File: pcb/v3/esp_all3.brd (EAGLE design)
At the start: 45 x 95 mm, 23 parts

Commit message: updated schematic
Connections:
- net N$25 renamed 3V3
- net N$26 renamed DHT_SIG
- net N$28 renamed TTL_DIMM
- removed net N$23: ESP.D5, ESP.D51
- removed net N$29: ESP.D1, ESP.D11, PIR.2
- new net N$16: ESP.D1, ESP.D11
- new net PIR: ESP.D5, ESP.D51, PIR.2
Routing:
- net PIR: track 0.00 -> 66.7 mm, vias 0 -> 2
- net N$29: track 51.9 -> 0.00 mm, vias 2 -> 0
- net N$23: track 2.47 -> 0.00 mm
- net N$16: track 0.00 -> 2.47 mm
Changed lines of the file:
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@@
 <wire x1="37.12" y1="25.18" x2="38.3" y2="24" width="0.4064" layer="1"/>
 </signal>
-<signal name="N$23">
+<signal name="PIR">
 <contactref element="ESP" pad="D5"/>
 <contactref element="ESP" pad="D51"/>
 <wire x1="31.1" y1="32.8" x2="28.63" y2="32.8" width="0.4064" layer="1"/>
-</signal>
-<signal name="N$26">
+<contactref element="PIR" pad="2"/>
+<wire x1="13.26" y1="48.04" x2="13.2" y2="48.1" width="0.4064" layer="1"/>
+<via x="13.2" y="48.1" extent="1-16" drill="0.3048"/>
+<wire x1="13.2" y1="48.1" x2="12.8" y2="48.5" width="0.4064" layer="16"/>
+<wire x1="12.8" y1="48.5" x2="12.8" y2="58.4" width="0.4064" layer="16"/>
+<wire x1="12.8" y1="58.4" x2="10.6" y2="60.6" width="0.4064" layer="16"/>
+<wire x1="28.63" y1="32.8" x2="29.9" y2="34.07" width="0.4064" layer="16"/>
+<wire x1="29.9" y1="34.07" x2="29.9" y2="46.8" width="0.4064" layer="16"/>
+<via x="29.9" y="46.8" extent="1-16" drill="0.3048"/>
+<wire x1="29.9" y1="46.8" x2="21.1" y2="46.8" width="0.4064" layer="1"/>
+<wire x1="21.1" y1="46.8" x2="19.8" y2="48.1" width="0.4064" layer="1"/>
+<wire x1="19.8" y1="48.1" x2="13.2" y2="48.1" width="0.4064" layer="1"/>
+<wire x1="10.6" y1="60.6" x2="10.6" y2="76.36" width="0.4064" layer="16"/>
+<wire x1="10.6" y1="76.36" x2="12.74" y2="78.5" width="0.4064" layer="16"/>
+</signal>
+<signal name="DHT_SIG">
 <contactref element="ESP" pad="D4"/>
 <contactref element="DHT22" pad="2"/>
@@
 <wire x1="15.396" y1="42.96" x2="15.1584" y2="43.1976" width="0.4064" layer="1"/>
 </signal>
-<signal name="N$28">
+<signal name="TTL_DIMM">
 <contactref element="ESP" pad="D2"/>
 <contactref element="DIMMING" pad="1"/>
@@
 <wire x1="19.8" y1="46.3" x2="20.6" y2="45.5" width="0.4064" layer="1"/>
 <wire x1="20.6" y1="45.5" x2="28.63" y2="45.5" width="0.4064" layer="1"/>
-</signal>
-<signal name="N$29">
-<contactref element="ESP" pad="D1"/>
-<contactref element="PIR" pad="2"/>
-<contactref element="ESP" pad="D11"/>
-<wire x1="31.1" y1="48.04" x2="28.63" y2="48.04" width="0.4064" layer="1"/>
-<wire x1="28.63" y1="48.04" x2="13.26" y2="48.04" width="0.4064" layer="1"/>
-<wire x1="13.26" y1="48.04" x2="13.2" y2="48.1" width="0.4064" layer="1"/>
-<via x="13.2" y="48.1" extent="1-16" drill="0.3048"/>
-<wire x1="13.2" y1="48.1" x2="12.8" y2="48.5" width="0.4064" layer="16"/>
-<wire x1="12.8" y1="48.5" x2="12.8" y2="58.4" width="0.4064" layer="16"/>
-<wire x1="12.8" y1="58.4" x2="10.6" y2="60.6" width="0.4064" layer="16"/>
-<via x="10.6" y="60.6" extent="1-16" drill="0.3048"/>
-<wire x1="8.7" y1="71.8" x2="8.7" y2="74.46" width="0.4064" layer="1"/>
-<wire x1="8.7" y1="74.46" x2="12.74" y2="78.5" width="0.4064" layer="1"/>
-<wire x1="10.6" y1="60.6" x2="9.7" y2="61.5" width="0.4064" layer="1"/>
-<wire x1="9.7" y1="61.5" x2="9.7" y2="70.8" width="0.4064" layer="1"/>
-<wire x1="9.7" y1="70.8" x2="8.7" y2="71.8" width="0.4064" layer="1"/>
 </signal>
 <signal name="N$30">
@@
 <contactref element="ESP" pad="3V3@2"/>
 </signal>
-<signal name="N$25">
+<signal name="3V3">
 <contactref element="SV3" pad="1"/>
 <contactref element="SV2" pad="1"/>
@@
 <wire x1="12.8" y1="13.9" x2="12.9" y2="13.8" width="0.4064" layer="1"/>
 </signal>
+<signal name="N$16">
+<contactref element="ESP" pad="D1"/>
+<contactref element="ESP" pad="D11"/>
+<wire x1="31.1" y1="48.04" x2="28.63" y2="48.04" width="0.4064" layer="1"/>
+</signal>
 </signals>

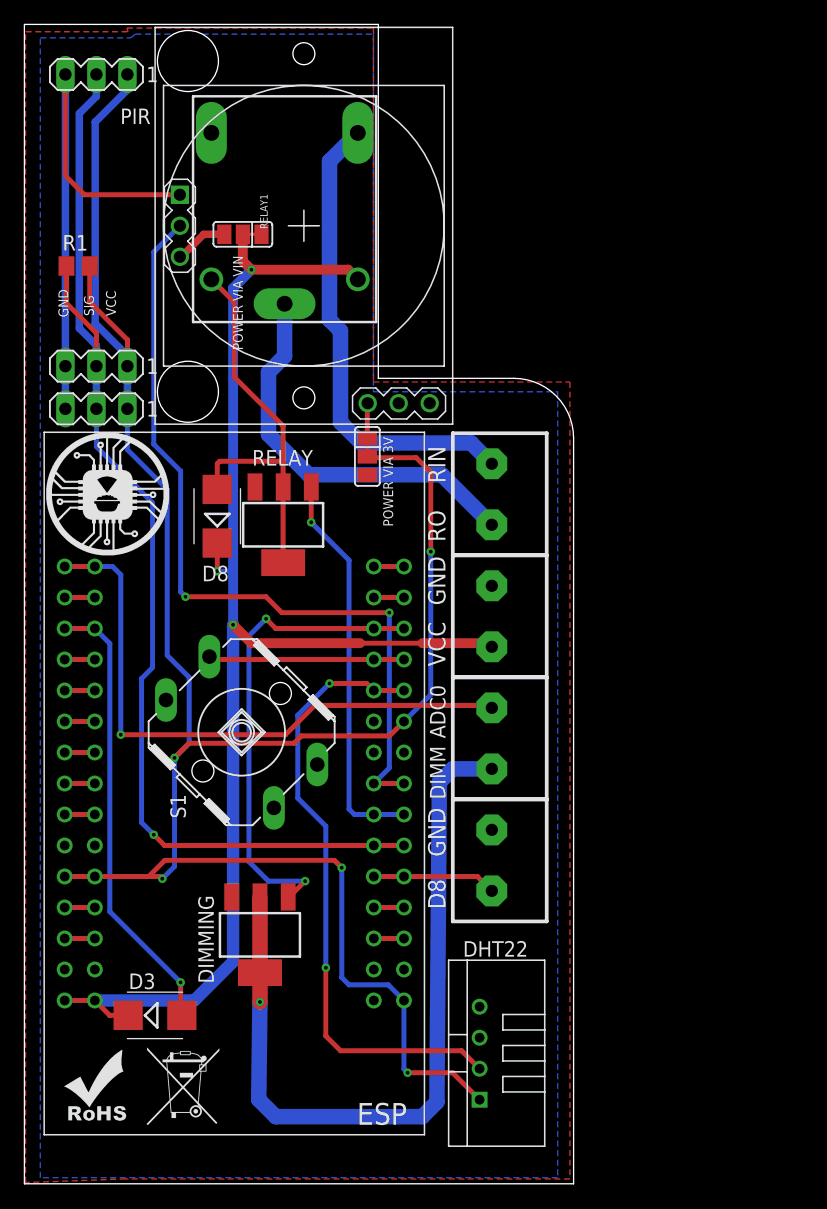
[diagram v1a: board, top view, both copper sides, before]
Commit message: added LDO
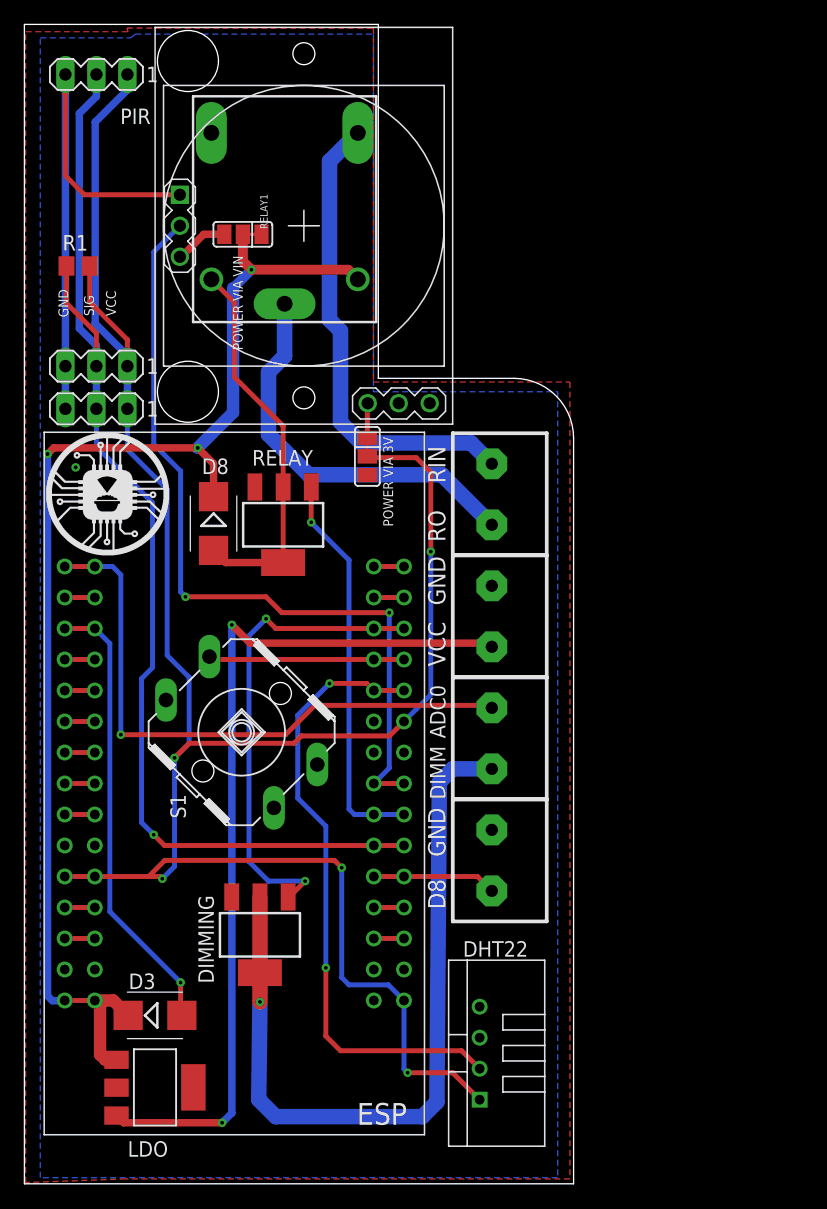
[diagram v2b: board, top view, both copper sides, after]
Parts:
- added LDO: REG1118, burr-brown:SOT223
- moved U$4 25.5 mm to (35.2, 1.20), flipped to the bottom
- moved U$9 23.3 mm to (25.8, 1.50), flipped to the bottom
- moved D8 0.67 mm to (15.5, 54.1), turned to 270 degrees
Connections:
- new net N$17: LDO.3, U$7.P$1
- net GND: now also LDO.2
- net VCC: now also LDO.1; no longer U$7.P$1
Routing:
- net N$17: track 0.00 -> 72.1 mm, vias 0 -> 2
- net VCC: track 113.9 -> 103.5 mm
- net RELAY_LO3: track 33.3 -> 31.9 mm
- net GND: vias 0 -> 1
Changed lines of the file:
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@@
 <text x="41" y="52.6" size="1.4224" layer="26" font="vector" rot="MR90">RO</text>
 <text x="41" y="57.4" size="1.4224" layer="26" font="vector" rot="MR90">RIN</text>
-<text x="16.9" y="2.6" size="1.778" layer="26" font="vector" rot="MR0">SMARTHOME
+<text x="17" y="1.7" size="1.778" layer="26" font="vector" rot="MR0">SMARTHOME
 ESP MQTT
 v03 | 2017</text>
@@
 <attribute name="VALUE" x="23.74" y="55.3208" size="1.27" layer="27" rot="R180"/>
 </element>
-<element name="D8" library="diode" package="SMB" value="ES2D" x="15.8" y="54.7" smashed="yes" rot="R90">
-<attribute name="NAME" x="16.759" y="50.641" size="1.27" layer="25" rot="R180"/>
-<attribute name="VALUE" x="19.229" y="52.541" size="1.27" layer="27" rot="R90"/>
+<element name="D8" library="diode" package="SMB" value="ES2D" x="15.5" y="54.1" smashed="yes" rot="R270">
+<attribute name="NAME" x="14.541" y="58.159" size="1.27" layer="25"/>
+<attribute name="VALUE" x="12.071" y="56.259" size="1.27" layer="27" rot="R270"/>
 </element>
 <element name="U$8" library="JKW_CHIP" package="2_SCREW_PIN" value="V1" x="38.8" y="56.5" rot="R90"/>
@@
 </element>
 <element name="U$1" library="JKW_CHIP" package="LOGO2_10X10_SILK" value="LOGO_10X10_SILK" x="18.8" y="17.4" rot="MR0"/>
-<element name="U$4" library="JKW_CHIP" package="LOGO_ROHS_NO_TRASH" value="LOGO_NO_TRASHNO_TRASH" x="10" y="4.8"/>
-<element name="U$9" library="JKW_CHIP" package="LOGO_ROHS_SYM" value="LOGO_NO_TRASHROHS" x="2.8" y="5.1"/>
+<element name="U$4" library="JKW_CHIP" package="LOGO_ROHS_NO_TRASH" value="LOGO_NO_TRASHNO_TRASH" x="35.2" y="1.2" rot="MR0"/>
+<element name="U$9" library="JKW_CHIP" package="LOGO_ROHS_SYM" value="LOGO_NO_TRASHROHS" x="25.8" y="1.5" rot="MR0"/>
 <element name="U$11" library="JKW_CHIP" package="LOGO2_10X10_SILK" value="LOGO_10X10_SILK" x="1.8" y="51.5"/>
 <element name="D3" library="diode" package="SMB" value="ES2D" x="10.7" y="13.8"/>
+<element name="LDO" library="burr-brown" package="SOT223" value="REG1118" x="10.7" y="7.9" smashed="yes" rot="R270">
+<attribute name="MPN" value="REG1118-2.85/2K5G4" x="10.7" y="7.9" size="1.778" layer="27" rot="R270" display="off"/>
+<attribute name="OC_NEWARK" value="14M2185" x="10.7" y="7.9" size="1.778" layer="27" rot="R270" display="off"/>
+<attribute name="OC_FARNELL" value="unknown" x="10.7" y="7.9" size="1.778" layer="27" rot="R270" display="off"/>
+<attribute name="MF" value="" x="10.7" y="7.9" size="1.778" layer="27" rot="R270" display="off"/>
+<attribute name="NAME" x="8.46" y="2.218" size="1.27" layer="25" ratio="10"/>
+<attribute name="VALUE" x="4.858" y="10.694" size="1.27" layer="27" ratio="10" rot="R270"/>
+</element>
 </elements>
 <signals>
@@
 <wire x1="12.74" y1="81.04" x2="4.92" y2="81.04" width="0.4064" layer="1"/>
 <wire x1="4.92" y1="81.04" x2="3.36" y2="82.6" width="0.4064" layer="1"/>
+<contactref element="LDO" pad="2"/>
+<via x="4.2" y="58.7" extent="1-16" drill="0.3084"/>
 </signal>
 <signal name="VCC">
 <contactref element="D8" pad="C"/>
 <contactref element="RELAY1" pad="COIL0"/>
-<contactref element="U$7" pad="P$1"/>
 <contactref element="U$6" pad="2"/>
-<via x="17.1" y="45.8" extent="1-16" drill="0.3048"/>
-<wire x1="17.1" y1="50.1" x2="17.1" y2="45.8" width="0.8128" layer="16"/>
-<wire x1="38.3" y1="44" x2="38" y2="44.3" width="0.4064" layer="1"/>
-<wire x1="15.8" y1="52.5" x2="15.8" y2="50.2" width="0.4064" layer="1"/>
-<via x="15.8" y="50.2" extent="1-16" drill="0.3048"/>
-<wire x1="15.8" y1="50.2" x2="17" y2="50.2" width="0.4064" layer="16"/>
-<wire x1="17" y1="50.2" x2="17.1" y2="50.1" width="0.4064" layer="16"/>
-<wire x1="17.1" y1="45.8" x2="18.6" y2="44.3" width="0.8128" layer="1"/>
-<wire x1="18.6" y1="44.3" x2="27.5" y2="44.3" width="0.8128" layer="1"/>
-<wire x1="27.5" y1="44.3" x2="32.6" y2="44.3" width="0.4064" layer="1"/>
-<wire x1="32.6" y1="44.3" x2="38" y2="44.3" width="0.8128" layer="1"/>
-<wire x1="38" y1="44.3" x2="38.3" y2="44" width="0.8128" layer="1" curve="-90"/>
 <contactref element="ESP" pad="VIN"/>
 <contactref element="ESP" pad="VIN1"/>
 <contactref element="D3" pad="C"/>
-<wire x1="8.5" y1="13.8" x2="6.99" y2="13.8" width="0.4064" layer="1"/>
-<wire x1="6.99" y1="13.8" x2="5.77" y2="15.02" width="0.4064" layer="1"/>
 <wire x1="5.77" y1="15.02" x2="3.3" y2="15.02" width="0.4064" layer="1"/>
-<wire x1="5.77" y1="15.02" x2="13.92" y2="15.02" width="1.016" layer="16"/>
-<wire x1="13.92" y1="15.02" x2="17.1" y2="18.2" width="1.016" layer="16"/>
-<wire x1="17.1" y1="18.2" x2="17.1" y2="45.8" width="1.016" layer="16"/>
-<wire x1="17.1" y1="50.1" x2="17.1" y2="73.4" width="0.8128" layer="16"/>
 <wire x1="17.1" y1="73.4" x2="18.6" y2="74.9" width="0.8128" layer="16"/>
 <via x="18.6" y="74.9" extent="1-16" drill="0.3048"/>
@@
 <wire x1="18.6" y1="74.9" x2="17.9" y2="75.6" width="0.8128" layer="1"/>
 <wire x1="17.9" y1="75.6" x2="17.9" y2="77.8" width="0.8128" layer="1"/>
+<contactref element="LDO" pad="1"/>
+<wire x1="7.5504" y1="10.1606" x2="6.6394" y2="10.1606" width="1.016" layer="1"/>
+<wire x1="6.6394" y1="10.1606" x2="6.2" y2="10.6" width="1.016" layer="1"/>
+<wire x1="6.2" y1="10.6" x2="6.2" y2="14.59" width="1.016" layer="1"/>
+<wire x1="6.2" y1="14.59" x2="5.77" y2="15.02" width="1.016" layer="1"/>
+<wire x1="17.1" y1="73.4" x2="17.1" y2="63.2" width="1.016" layer="16"/>
+<wire x1="17.1" y1="63.2" x2="14.2" y2="60.3" width="1.016" layer="16"/>
+<via x="14.2" y="60.3" extent="1-16" drill="0.3084"/>
+<wire x1="14.2" y1="60.3" x2="2.4" y2="60.3" width="0.6096" layer="1"/>
+<wire x1="2.4" y1="60.3" x2="1.9" y2="59.8" width="0.6096" layer="1"/>
+<via x="1.9" y="59.8" extent="1-16" drill="0.3084"/>
+<wire x1="1.9" y1="59.8" x2="1.9" y2="15.4" width="0.6096" layer="16"/>
+<wire x1="1.9" y1="15.4" x2="2.3" y2="15" width="0.6096" layer="16"/>
+<wire x1="2.3" y1="15" x2="3.28" y2="15" width="0.6096" layer="16"/>
+<wire x1="3.28" y1="15" x2="3.3" y2="15.02" width="0.6096" layer="16"/>
+<wire x1="15.5" y1="56.3" x2="15.5" y2="59" width="0.6096" layer="1"/>
+<wire x1="15.5" y1="59" x2="14.2" y2="60.3" width="0.6096" layer="1"/>
+<wire x1="8.5" y1="13.8" x2="7.28" y2="15.02" width="1.016" layer="1"/>
+<wire x1="7.28" y1="15.02" x2="5.77" y2="15.02" width="1.016" layer="1"/>
 </signal>
 <signal name="RELAY_LO3">
@@
 <wire x1="21.2" y1="57.099" x2="21.2" y2="59.1" width="0.4064" layer="1"/>
 <wire x1="21.2" y1="57.099" x2="21.2" y2="50.901" width="0.4064" layer="1"/>
-<wire x1="15.8" y1="56.9" x2="15.8" y2="59" width="0.4064" layer="1"/>
-<wire x1="15.8" y1="59" x2="16" y2="59.2" width="0.4064" layer="1"/>
-<wire x1="16" y1="59.2" x2="21.1" y2="59.2" width="0.4064" layer="1"/>
 <wire x1="21.1" y1="59.2" x2="21.2" y2="59.1" width="0.4064" layer="1"/>
 <wire x1="21.2" y1="59.1" x2="21.2" y2="62.1" width="0.4064" layer="1"/>
@@
 <wire x1="17.2" y1="72.23" x2="17.2" y2="66.1" width="0.4064" layer="1"/>
 <wire x1="17.2" y1="66.1" x2="21.2" y2="62.1" width="0.4064" layer="1"/>
+<wire x1="15.5" y1="51.9" x2="16.499" y2="50.901" width="0.6096" layer="1"/>
+<wire x1="16.499" y1="50.901" x2="21.2" y2="50.901" width="0.6096" layer="1"/>
 </signal>
 <signal name="NORMALLY_OPEN">
@@
 <wire x1="31.1" y1="48.04" x2="28.63" y2="48.04" width="0.4064" layer="1"/>
 </signal>
+<signal name="N$17">
+<contactref element="U$7" pad="P$1"/>
+<contactref element="LDO" pad="3"/>
+<wire x1="38.3" y1="44" x2="38" y2="44.3" width="0.6096" layer="1"/>
+<wire x1="38" y1="44.3" x2="18.5" y2="44.3" width="0.6096" layer="1"/>
+<wire x1="18.5" y1="44.3" x2="17" y2="45.8" width="0.6096" layer="1"/>
+<via x="17" y="45.8" extent="1-16" drill="0.3084"/>
+<wire x1="17" y1="45.8" x2="17" y2="5.8" width="0.6096" layer="16"/>
+<wire x1="17" y1="5.8" x2="16.2" y2="5" width="0.6096" layer="16"/>
+<via x="16.2" y="5" extent="1-16" drill="0.3084"/>
+<wire x1="16.2" y1="5" x2="8.139" y2="5" width="0.6096" layer="1"/>
+<wire x1="8.139" y1="5" x2="7.5504" y2="5.5886" width="0.6096" layer="1"/>
+</signal>
 </signals>

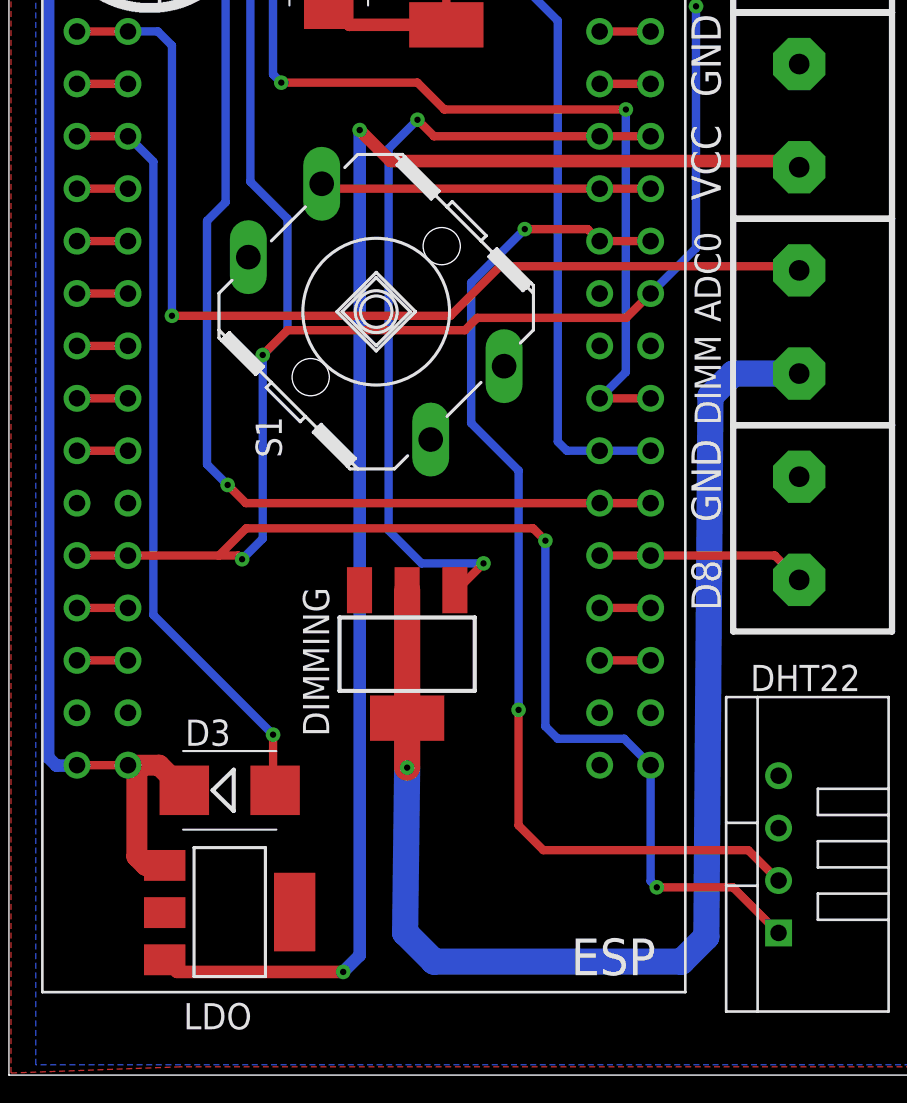
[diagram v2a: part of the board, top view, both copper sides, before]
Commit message: added double footprint for power transistor
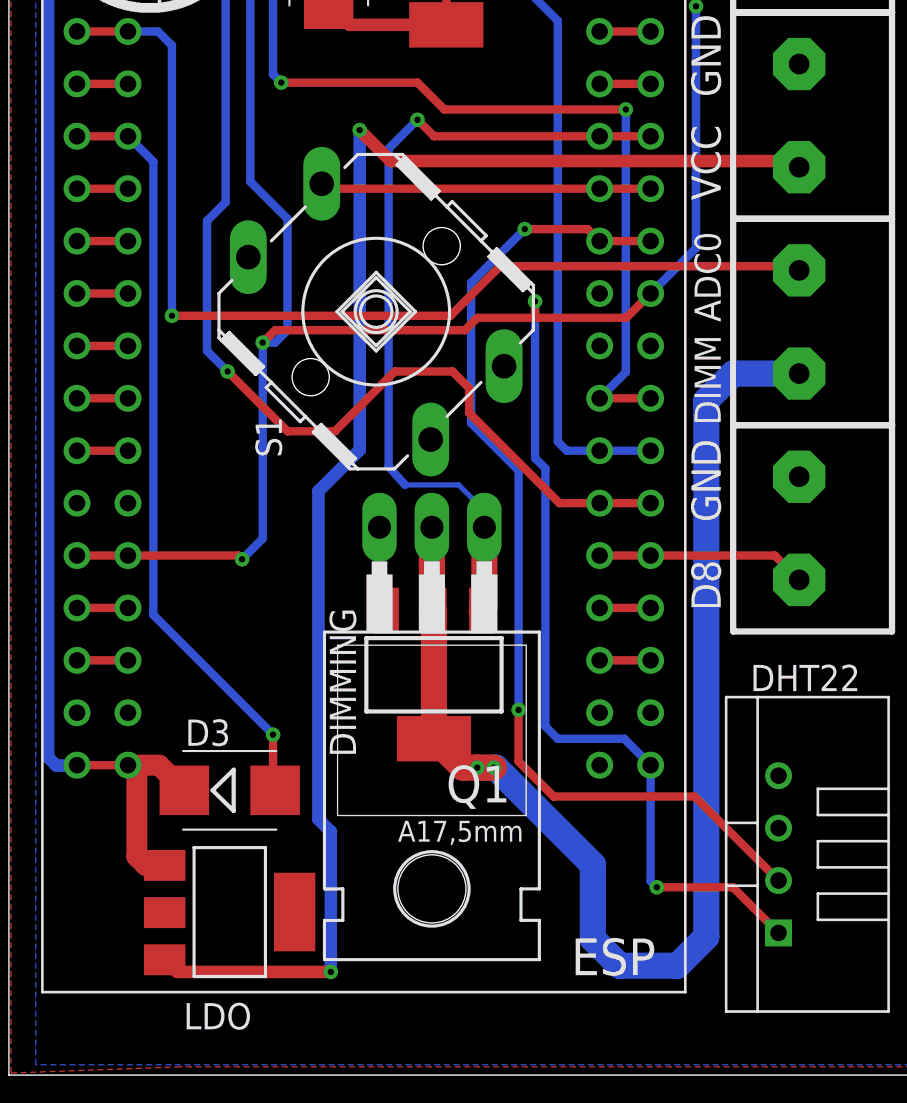
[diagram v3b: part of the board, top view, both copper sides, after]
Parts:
- added Q1: BUZ11BH, transistor-power:TO220BH
- moved U$9 2.92 mm to (28.7, 1.20)
- moved DIMMING 1.64 mm to (20.6, 19.4)
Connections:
- net DIMMING: now also Q1.D
- net GND: now also Q1.S
- net TTL_DIMM: now also Q1.G
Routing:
- net 3V3: track 180.1 -> 176.2 mm
- net DHT_SIG: track 51.0 -> 49.2 mm
- net DIMMING: track 63.2 -> 62.8 mm, vias 1 -> 2
- net TTL_DIMM: track 39.3 -> 39.5 mm, vias 2 -> 1
